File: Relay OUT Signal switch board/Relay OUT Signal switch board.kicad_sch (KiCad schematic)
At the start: 18 parts, among them IC1 ULN2003LVDR, J1 1725672, J2 1725672, J3 SE Out, J4 R_Bal_out, J5 Left Bal out, J6 Right 2, J7 Right 1, J8 Left 1, J9 Left 2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

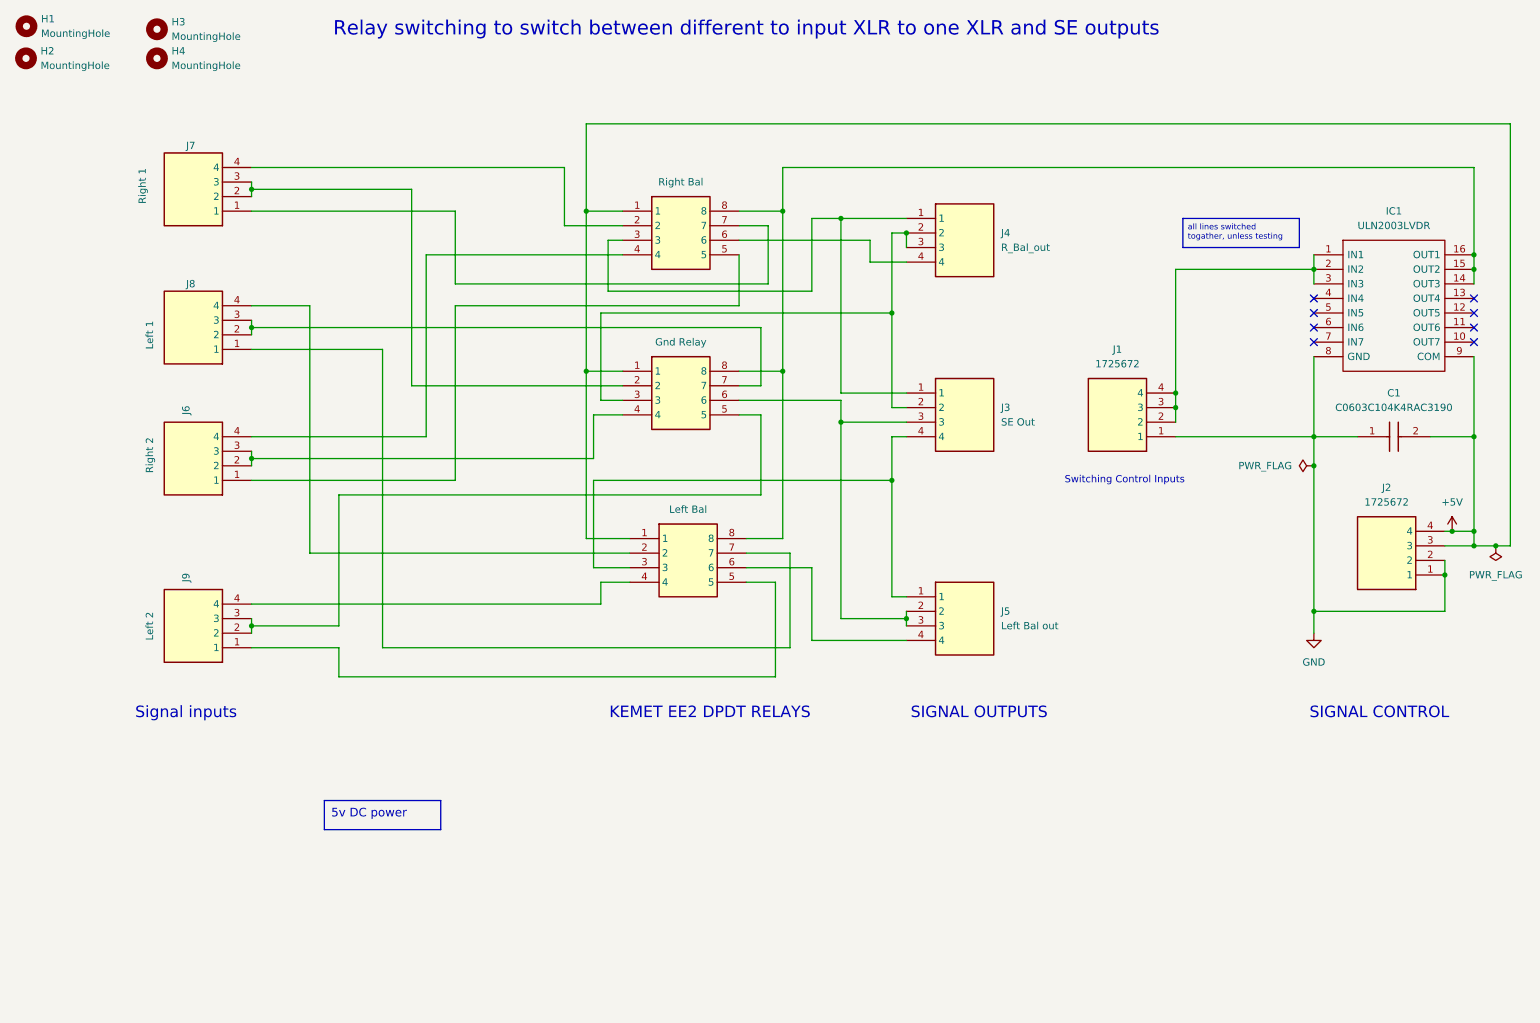
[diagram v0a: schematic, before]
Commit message: update relayboard set size for RPI4
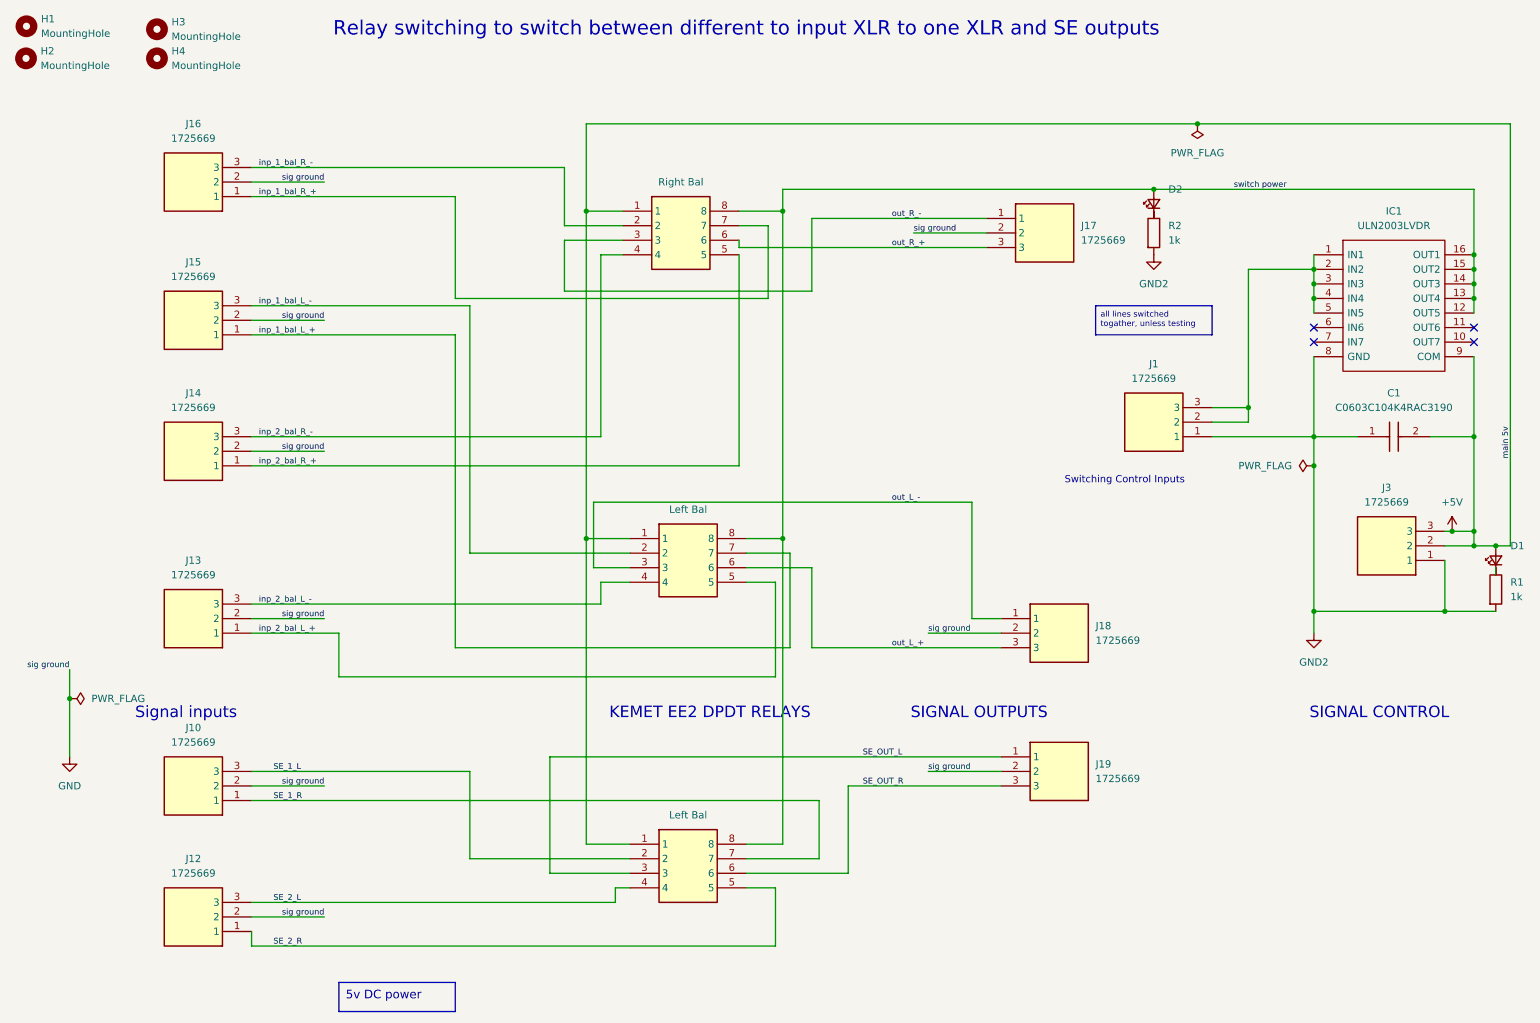
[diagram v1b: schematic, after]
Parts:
- removed J1, J2: 1725672, 1725672, symbol NewSamsys:1725672
- removed J3: SE Out, 1725672, symbol NewSamsys:1725672
- removed J4: R_Bal_out, 1725672, symbol NewSamsys:1725672
- removed J5: Left Bal out, 1725672, symbol NewSamsys:1725672
- removed J6: Right 2, 1725672, symbol NewSamsys:1725672
- removed J7: Right 1, 1725672, symbol NewSamsys:1725672
- removed J8: Left 1, 1725672, symbol NewSamsys:1725672
- removed J9: Left 2, 1725672, symbol NewSamsys:1725672
- removed K2: Gnd Relay, EE2-5NU, symbol NewSamsys:EE2-5NU
- added D1, D2: LS_R976, samsys:LEDC2012X40N, symbol Device:LED_Small
- added J1, J10, J12, J13, J14, J15, J16, J17, J18, J19, J3: 1725669, 1725669, symbol NewSamsys:1725669
- added K4: Left Bal, EE2-5NU, symbol NewSamsys:EE2-5NU
- added R1, R2: 1k, Resistor_SMD:R_0603_1608Metric, symbol Device:R
- C1: footprint K104K20X7RK53H5G -> Capacitor_SMD:C_0603_1608Metric
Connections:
- net +5V: now also D1.2 (A), J3.2, J3.3, K4.1
- net GND: now also J10.2, J12.2, J13.2, J14.2, J15.2, J16.2, J17.2, J18.2, J19.2; no longer C1.1, IC1.8 (GND)
- net out_L_-: now reaches K1.3
- net out_L_-: now also J18.1
- net out_L_+: now reaches K1.6
- net out_L_+: now also J18.3
- net out_R_-: now reaches K3.3
- net out_R_-: now also J17.1
- net inp_1_bal_R_+: now reaches K3.7
- net inp_1_bal_R_+: now also J16.1
- net inp_1_bal_R_-: now reaches K3.2
- net inp_1_bal_R_-: now also J16.3
- net inp_2_bal_L_+: now reaches K1.5
- net inp_2_bal_L_+: now also J13.1
- net inp_2_bal_L_-: now reaches K1.4
- net inp_2_bal_L_-: now also J13.3
- net at IC1.1 (IN1), IC1.2 (IN2), IC1.3 (IN3): now also IC1.4 (IN4), IC1.5 (IN5), J1.2, J1.3
- net switch power: now reaches IC1.14 (OUT3), IC1.15 (OUT2), IC1.16 (OUT1), K1.8, K3.8
- net switch power: now also IC1.12 (OUT5), IC1.13 (OUT4), D2.2 (A), K4.8
- net inp_2_bal_R_+: now reaches K3.5
- net inp_2_bal_R_+: now also J14.1
- net inp_2_bal_R_-: now reaches K3.4
- net inp_2_bal_R_-: now also J14.3
- net inp_1_bal_L_-: now reaches K1.2
- net inp_1_bal_L_-: now also J15.3
- net inp_1_bal_L_+: now reaches K1.7
- net inp_1_bal_L_+: now also J15.1
- net out_R_+: now reaches K3.6
- net out_R_+: now also J17.3
- new net: D1.1 (K), R1.1
- new net GND2: C1.1, IC1.8 (GND), J1.1, J3.1, R1.2, R2.2
- new net SE_1_L: J10.3, K4.2
- new net SE_1_R: J10.1, K4.7
- new net SE_2_L: J12.3, K4.4
- new net SE_2_R: J12.1, K4.5
- new net SE_OUT_L: J19.1, K4.3
- new net SE_OUT_R: J19.3, K4.6
- no-connect marks 8 -> 4

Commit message: add updates to se to diff
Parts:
- removed K1, K4: Left Bal, EE2-5NU, symbol NewSamsys:EE2-5NU
- removed K3: Right Bal, EE2-5NU, symbol NewSamsys:EE2-5NU
- added K1, K2, K3: EC2-5SNU, Relay_THT:Relay_DPDT_Kemet_EC2, symbol Relay:EC2-5SNU
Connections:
- net +5V: now also K1.1, K2.1, K3.1
- net SE_1_L: now also K3.3
- net SE_1_R: now also K3.10
- net SE_2_L: now also K3.5
- net SE_2_R: now also K3.8
- net SE_OUT_L: no longer J19.1
- net inp_1_bal_L_+: now also J15.3, K1.10; no longer J15.1
- net inp_1_bal_L_-: now also J15.1, K1.3; no longer J15.3
- net inp_1_bal_R_+: now also J16.3, K2.10; no longer J16.1
- net inp_1_bal_R_-: now also J16.1, K2.3; no longer J16.3
- net inp_2_bal_L_+: now also K1.8
- net inp_2_bal_L_-: now also K1.5
- net inp_2_bal_R_+: now also K2.8
- net inp_2_bal_R_-: now also K2.5
- net out_L_+: no longer J18.3
- net out_L_-: no longer J18.1
- net out_R_+: no longer J17.3
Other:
- note added: "Left Balanced switch"
- note added: "Right Balanced switch"
- note added: "SE Balanced switch"
- note removed: "KEMET EE2 DPDT RELAYS"
- moved on the sheet: D2, J10, J12, J13, J15, J16, R2

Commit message: updated final four boards for streamer
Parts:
- added J2: Conn_01x01_Socket, Connector_PinHeader_1.00mm:PinHeader_1x01_P1.00mm_Vertical, symbol Connector:Conn_01x01_Socket
- added R3: 10R, Resistor_SMD:R_0603_1608Metric, symbol Device:R
- C1: value C0603C104K4RAC3190 -> 0.1
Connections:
- net GND2: now also R3.2
- net SE_1_L: now also J10.1; no longer J10.3
- net SE_1_R: now also J10.3; no longer J10.1
- net SE_2_L: now also J12.1; no longer J12.3
- net SE_2_R: now also J12.3; no longer J12.1
- net SE_OUT_L: now also J19.3, K3.4
- net SE_OUT_R: now also J19.1, K3.9; no longer J19.3
- net inp_2_bal_L_+: now also J13.3; no longer J13.1
- net inp_2_bal_L_-: now also J13.1; no longer J13.3
- net inp_2_bal_R_+: now also J14.3; no longer J14.1
- net inp_2_bal_R_-: now also J14.1; no longer J14.3
- net out_L_+: now also J18.1, K1.9
- net out_L_-: now also J18.3, K1.4
- net out_R_+: now also J17.1, K2.9
- net out_R_-: now also J17.3, K2.4; no longer J17.1
- net switch power: now also K1.12, K2.12, K3.12
- net at R2.1: now also D2.1 (K)
- net GND renamed sig ground
- net sig ground: now also R3.1
- new net Earth: J2.1 (Pin_1)
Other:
- note added: "Power"
- note added: "Single ended out"
- note added: "Switching"
- note added: "out balanced Left"
- note added: "out balanced Right"
- note removed: "Switching Control Inputs"
- moved on the sheet: C1, D1, D2, H1, H2, H3, H4, IC1, J1, J10, J12, J13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

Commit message: More changes to the boards
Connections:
- net switch power: no longer D2.2 (A)
- net at IC1.1 (IN1), IC1.2 (IN2), IC1.3 (IN3)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: now also D2.2 (A)
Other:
- moved on the sheet: D2, R2
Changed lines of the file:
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@@
 	)
 	(junction
-		(at 204.47 86.36)
+		(at 243.84 85.09)
 		(diameter 0)
 		(color 0 0 0 0)
 	)
 	(junction
-		(at 243.84 85.09)
+		(at 243.84 67.31)
 		(diameter 0)
 		(color 0 0 0 0)
 	)
 	(junction
-		(at 243.84 67.31)
+		(at 207.01 62.23)
 		(diameter 0)
 		(color 0 0 0 0)
@@
 	)
 	(junction
-		(at 194.31 48.26)
+		(at 207.01 86.36)
 		(diameter 0)
 		(color 0 0 0 0)
@@
 	(wire
 		(pts
-			(xy 215.9 62.23) (xy 204.47 62.23)
+			(xy 215.9 62.23) (xy 207.01 62.23)
 		)
 		(stroke
@@
 	(wire
 		(pts
-			(xy 125.73 107.95) (xy 125.73 113.03)
+			(xy 199.39 62.23) (xy 207.01 62.23)
 		)
 		(stroke
@@
 	(wire
 		(pts
-			(xy 215.9 77.47) (xy 215.9 91.44)
+			(xy 125.73 107.95) (xy 125.73 113.03)
 		)
 		(stroke
@@
 	(wire
 		(pts
-			(xy 190.5 53.34) (xy 194.31 53.34)
+			(xy 215.9 77.47) (xy 215.9 91.44)
 		)
 		(stroke
@@
 	(wire
 		(pts
-			(xy 194.31 48.26) (xy 243.84 48.26)
-		)
-		(stroke
-			(width 0)
-			(type default)
-		)
-	)
-	(wire
-		(pts
-			(xy 198.12 86.36) (xy 204.47 86.36)
+			(xy 198.12 86.36) (xy 207.01 86.36)
 		)
 		(stroke
@@
 	(wire
 		(pts
-			(xy 181.61 48.26) (xy 194.31 48.26)
+			(xy 181.61 48.26) (xy 243.84 48.26)
 		)
 		(stroke
@@
 	(wire
 		(pts
-			(xy 190.5 60.96) (xy 190.5 62.23)
+			(xy 199.39 77.47) (xy 199.39 78.74)
 		)
 		(stroke
@@
 	(wire
 		(pts
+			(xy 199.39 64.77) (xy 199.39 62.23)
+		)
+		(stroke
+			(width 0)
+			(type default)
+		)
+	)
+	(wire
+		(pts
 			(xy 215.9 62.23) (xy 215.9 64.77)
 		)
@@
 	(wire
 		(pts
-			(xy 198.12 88.9) (xy 204.47 88.9)
+			(xy 198.12 88.9) (xy 207.01 88.9)
 		)
 		(stroke
@@
 	(wire
 		(pts
-			(xy 204.47 88.9) (xy 204.47 86.36)
+			(xy 207.01 88.9) (xy 207.01 86.36)
 		)
 		(stroke
@@
 	(wire
 		(pts
-			(xy 204.47 62.23) (xy 204.47 86.36)
+			(xy 207.01 62.23) (xy 207.01 86.36)
 		)
 		(stroke
@@
 	(text_box "all lines switched togather, unless testing"
 		(exclude_from_sim no)
-		(at 177.8 68.58 0)
+		(at 175.26 55.88 0)
 		(size 20.32 5.08)
 		(stroke
@@
 	(symbol
 		(lib_id "power:GND")
-		(at 190.5 62.23 0)
+		(at 199.39 78.74 0)
 		(unit 1)
 		(exclude_from_sim no)
@@
 		(fields_autoplaced yes)
 		(property "Reference" "#PWR03"
-			(at 190.5 68.58 0)
+			(at 199.39 85.09 0)
 			(effects
 				(font
@@
 		)
 		(property "Value" "GND2"
-			(at 190.5 67.31 0)
+			(at 199.39 83.82 0)
 			(effects
 				(font
@@
 		)
 		(property "Footprint" ""
-			(at 190.5 62.23 0)
+			(at 199.39 78.74 0)
 			(effects
 				(font
@@
 		)
 		(property "Datasheet" ""
-			(at 190.5 62.23 0)
+			(at 199.39 78.74 0)
 			(effects
 				(font
@@
 		)
 		(property "Description" "Power symbol creates a global label with name \"GND\" , ground"
-			(at 190.5 62.23 0)
+			(at 199.39 78.74 0)
 			(effects
 				(font
@@
 	(symbol
 		(lib_id "Device:R")
-		(at 190.5 57.15 0)
+		(at 199.39 73.66 0)
 		(unit 1)
 		(exclude_from_sim no)
@@
 		(fields_autoplaced yes)
 		(property "Reference" "R2"
-			(at 193.04 55.8799 0)
+			(at 201.93 72.3899 0)
 			(effects
 				(font
@@
 		)
 		(property "Value" "1k"
-			(at 193.04 58.4199 0)
+			(at 201.93 74.9299 0)
 			(effects
 				(font
@@
 		)
 		(property "Footprint" "Resistor_SMD:R_0603_1608Metric"
-			(at 188.722 57.15 90)
+			(at 197.612 73.66 90)
 			(effects
 				(font
@@
 		)
 		(property "Datasheet" "~"
-			(at 190.5 57.15 0)
+			(at 199.39 73.66 0)
 			(effects
 				(font
@@
 		)
 		(property "Description" "Resistor"
-			(at 190.5 57.15 0)
+			(at 199.39 73.66 0)
 			(effects
 				(font
@@
 	(symbol
 		(lib_id "Device:LED_Small")
-		(at 194.31 50.8 90)
+		(at 199.39 67.31 90)
 		(unit 1)
 		(exclude_from_sim no)
@@
 		(dnp no)
 		(property "Reference" "D2"
-			(at 196.85 48.26 90)
+			(at 201.93 64.77 90)
 			(effects
 				(font
@@
 		)
 		(property "Value" "LS_R976"
-			(at 196.85 52.0064 90)
+			(at 201.93 68.5164 90)
 			(effects
 				(font
@@
 		)
 		(property "Footprint" "samsys:LEDC2012X40N"
-			(at 287.96 38.1 0)
+			(at 293.04 54.61 0)
 			(effects
 				(font
@@
 		)
 		(property "Datasheet" "https://www.mouser.co.uk/datasheet/2/588/asset_pdf_5057921-3418987.pdf"
-			(at 387.96 38.1 0)
+			(at 393.04 54.61 0)
 			(effects
 				(font
@@
 		)
 		(property "Description" "Red 0805 CHIPLED LS R976N-R102 Osram Opto LS R976, CHIPLED 0805 Series Red LED, 633 nm, 2012 (0805), Rectangle Lens SMD Package"
-			(at 194.31 50.8 0)
+			(at 199.39 67.31 0)
 			(effects
 				(font
@@
 		)
 		(property "Height" "0.4"
-			(at 587.96 38.1 0)
+			(at 593.04 54.61 0)
 			(effects
 				(font
@@
 		)
 		(property "Mouser Part Number" "720-LSR976D5178"
-			(at 687.96 38.1 0)
+			(at 693.04 54.61 0)
 			(effects
 				(font
@@
 		)
 		(property "Mouser Price/Stock" "https://www.mouser.co.uk/ProductDetail/OSRAM-Opto-Semiconductors/LS-R976?qs=OIr7YF%252B2cWVTfzKl425Fkw%3D%3D"
-			(at 787.96 38.1 0)
+			(at 793.04 54.61 0)
 			(effects
 				(font
@@
 		)
 		(property "Manufacturer_Name" "ams OSRAM"
-			(at 887.96 38.1 0)
+			(at 893.04 54.61 0)
 			(effects
 				(font
@@
 		)
 		(property "Manufacturer_Part_Number" "LS R976"
-			(at 987.96 38.1 0)
+			(at 993.04 54.61 0)
 			(effects
 				(font
@@
 		)
 		(property "Mfr" ""
-			(at 194.31 50.8 0)
+			(at 199.39 67.31 0)
 			(effects
 				(font
@@
 		)
 		(property "mouser" ""
-			(at 194.31 50.8 0)
+			(at 199.39 67.31 0)
 			(effects
 				(font
